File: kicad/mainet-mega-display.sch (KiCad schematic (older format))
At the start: 0 parts

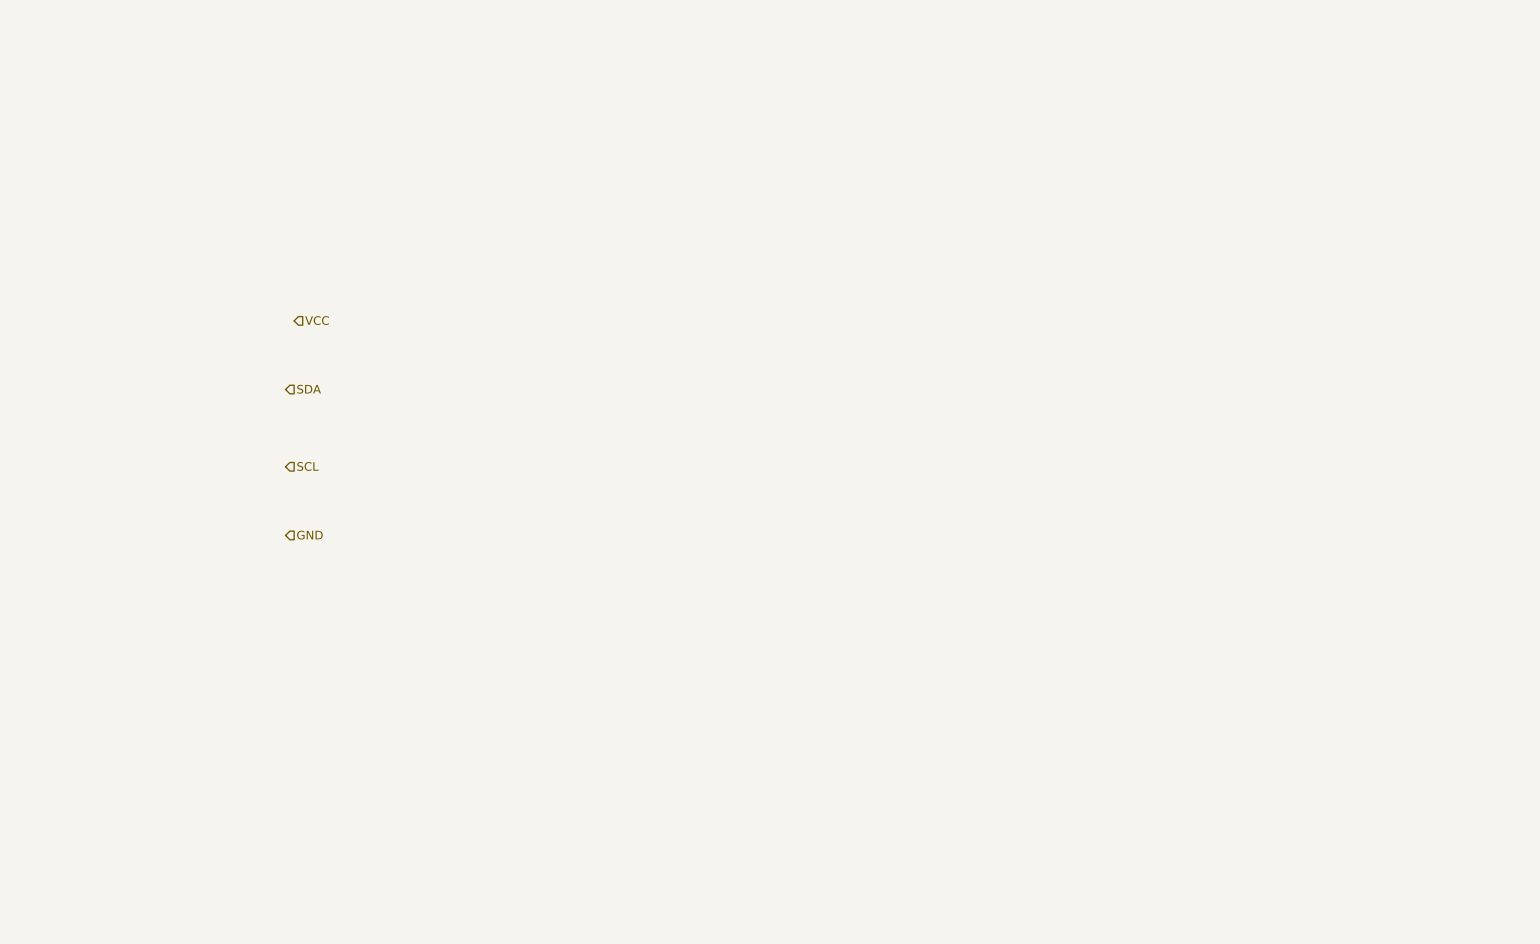
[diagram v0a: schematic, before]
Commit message: KICAD: Actualizar .sch del display Nextion
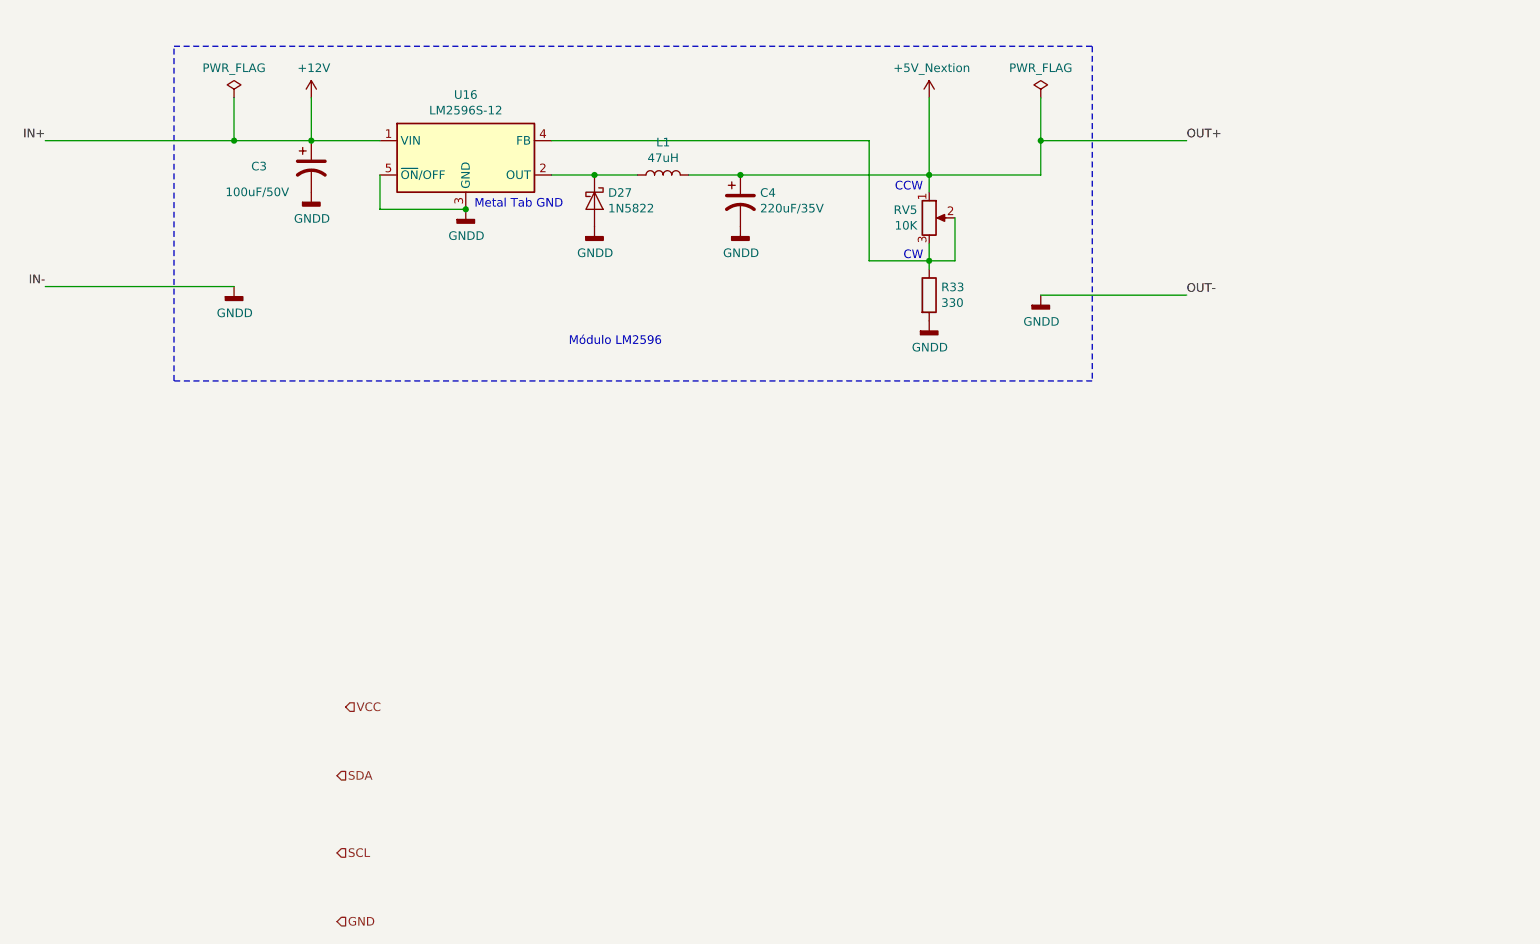
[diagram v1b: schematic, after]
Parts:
- added C3: 100uF/50V, symbol Device:CP1
- added C4: 220uF/35V, symbol Device:CP1
- added D27: 1N5822, Diode_THT:D_DO-201AD_P15.24mm_Horizontal, symbol Diode:1N5822
- added L1: 47uH, symbol Device:L
- added R33: 330, symbol Device:R
- added RV5: 10K, symbol Device:R_POT
- added U16: LM2596S-12, Package_TO_SOT_SMD:TO-263-5_TabPin3, symbol Regulator_Switching:LM2596S-12
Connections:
- new net: D27.1 (K), L1.2, U16.2 (OUT)
- new net: R33.1, RV5.2, RV5.3, U16.4 (FB)
- new net +12V: C3.1, U16.1 (VIN)
- new net +5V_Nextion: C4.1, L1.1, RV5.1
- new net GNDD: C3.2, C4.2, D27.2 (A), R33.2, U16.3 (GND), U16.5 (~ON~/OFF)
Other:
- note added: "CCW"
- note added: "CW"
- note added: "Metal Tab GND"
- note added: "Módulo LM2596"

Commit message: KICAD: Corregir pines de salida digital del Arduino para control de relés y pines de cableado con la pantalla Nextion
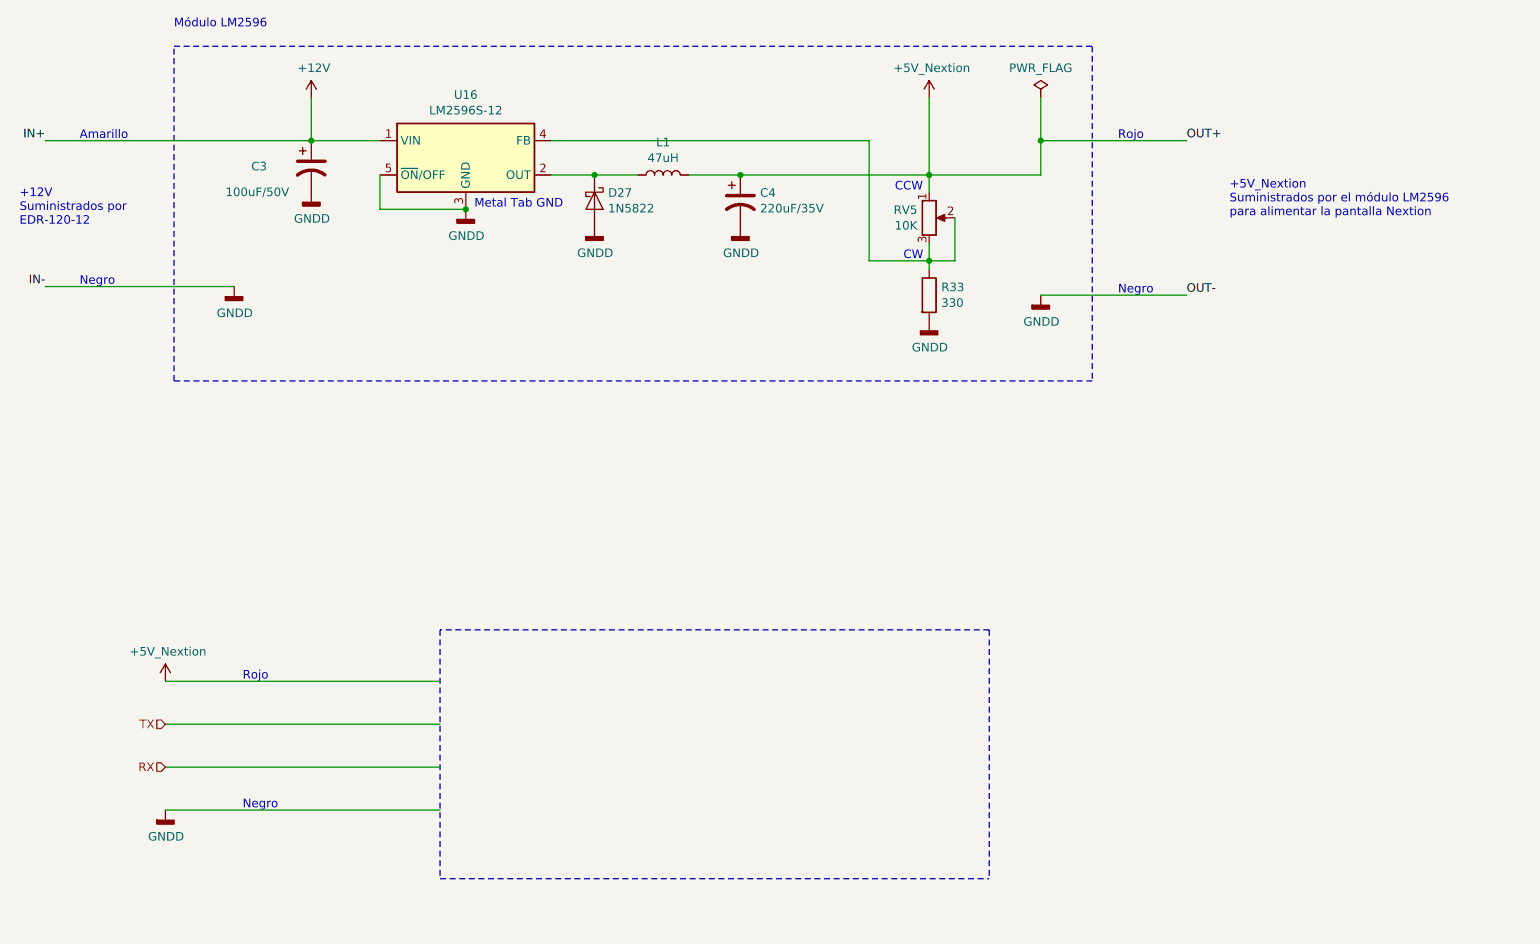
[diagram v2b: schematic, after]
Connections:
- net labels added: RX, TX
- net labels removed: GND, SCL, SDA, VCC
- wire segments 26 -> 28
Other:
- note added: "+12V\nSuministrados por\nEDR-120-12"
- note added: "+5V_Nextion\nSuministrados por el módulo LM2596\npara alimentar la pantalla Nextion"
- note added: "Amarillo"
- note added: "Negro"
- note added: "Rojo"
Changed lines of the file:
@@
 Comment4 ""
 $EndDescr
-Text HLabel 2850 4800 2    50   Input ~ 0
-VCC
-Text HLabel 2800 5200 2    50   Input ~ 0
-SDA
-Text HLabel 2800 5650 2    50   Input ~ 0
-SCL
-Text HLabel 2800 6050 2    50   Input ~ 0
-GND
+Text HLabel 1800 4900 0    50   Input ~ 0
+TX
+Text HLabel 1800 5150 0    50   Input ~ 0
+RX
 $Comp
 L nagar-power:+5V_Nextion #PWR048
@@
 	1    0    0    -1
 $EndComp
-Wire Wire Line
-	2200 1500 2650 1500
 Wire Wire Line
 	3050 1500 2650 1500
@@
 	6250 1700 6900 1700
 $Comp
-L power:PWR_FLAG #FLG0104
-U 1 1 60E05C43
-P 2200 1250
-F 0 "#FLG0104" H 2200 1325 50  0001 C CNN
-F 1 "PWR_FLAG" H 2200 1423 50  0000 C CNN
-F 2 "" H 2200 1250 50  0001 C CNN
-F 3 "~" H 2200 1250 50  0001 C CNN
-	1    2200 1250
-	1    0    0    -1
-$EndComp
-Wire Wire Line
-	2200 1250 2200 1500
-$Comp
 L power:+12V #PWR0107
 U 1 1 60E0E64F
@@
 Wire Notes Line
 	1850 2900 1850 950
-Text Notes 4150 2700 0    50   ~ 0
+Text Notes 1850 850  0    50   ~ 0
 Módulo LM2596
 Text Notes 6100 2200 0    50   ~ 0
@@
 Wire Wire Line
 	6900 2400 7750 2400
-Wire Wire Line
-	2200 1500 1100 1500
-Connection ~ 2200 1500
 Wire Wire Line
 	2200 2350 1100 2350
@@
 Text Notes 3600 1900 0    50   ~ 0
 Metal Tab GND
+Wire Wire Line
+	1100 1500 2650 1500
+Text Notes 1300 1500 0    50   ~ 0
+Amarillo
+Text Notes 1300 2350 0    50   ~ 0
+Negro
+Text Notes 7350 2400 0    50   ~ 0
+Negro
+Text Notes 7350 1500 0    50   ~ 0
+Rojo
+Wire Notes Line
+	3400 5800 6600 5800
+Wire Notes Line
+	6600 4350 3400 4350
+Wire Wire Line
+	1800 5150 3400 5150
+Wire Wire Line
+	3400 5400 1800 5400
+Text Notes 8000 1950 0    50   ~ 0
++5V_Nextion\nSuministrados por el módulo LM2596\npara alimentar la pantalla Nextion
+Text Notes 950  2000 0    50   ~ 0
++12V\nSuministrados por\nEDR-120-12
+Wire Wire Line
+	1800 4900 3400 4900
+Wire Notes Line
+	3400 4350 3400 5800
+Wire Notes Line
+	6600 4350 6600 5800
+$Comp
+L power:GNDD #PWR?
+U 1 1 60E37013
+P 1800 5400
+F 0 "#PWR?" H 1800 5150 50  0001 C CNN
+F 1 "GNDD" H 1804 5245 50  0000 C CNN
+F 2 "" H 1800 5400 50  0001 C CNN
+F 3 "" H 1800 5400 50  0001 C CNN
+	1    1800 5400
+	1    0    0    -1
+$EndComp
+$Comp
+L nagar-power:+5V_Nextion #PWR?
+U 1 1 60E37DCC
+P 1800 4650
+F 0 "#PWR?" H 1800 4500 50  0001 C CNN
+F 1 "+5V_Nextion" H 1815 4823 50  0000 C CNN
+F 2 "" H 1800 4650 50  0001 C CNN
+F 3 "" H 1800 4650 50  0001 C CNN
+	1    1800 4650
+	1    0    0    -1
+$EndComp
+Wire Wire Line
+	1800 4650 3400 4650
+Text Notes 2250 4650 0    50   ~ 0
+Rojo
+Text Notes 2250 5400 0    50   ~ 0
+Negro
 $EndSCHEMATC

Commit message: KICAD: Agregar correciones sch
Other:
- note added: "+5V"
- note added: "Azul"
- note added: "GND"
- note added: "RX"
- note added: "TX"
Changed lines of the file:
@@
 Sheet 3 22
 Title "Mainet-mega -- Diagrama de Conexiones Pantalla Nextion"
-Date "2021-04-07"
+Date "2021-07-02"
 Rev "1.0"
 Comp "Tovenca"
@@
 	6600 4350 6600 5800
 $Comp
-L power:GNDD #PWR?
+L power:GNDD #PWR0111
 U 1 1 60E37013
 P 1800 5400
-F 0 "#PWR?" H 1800 5150 50  0001 C CNN
+F 0 "#PWR0111" H 1800 5150 50  0001 C CNN
 F 1 "GNDD" H 1804 5245 50  0000 C CNN
 F 2 "" H 1800 5400 50  0001 C CNN
@@
 $EndComp
 $Comp
-L nagar-power:+5V_Nextion #PWR?
+L nagar-power:+5V_Nextion #PWR0112
 U 1 1 60E37DCC
 P 1800 4650
-F 0 "#PWR?" H 1800 4500 50  0001 C CNN
+F 0 "#PWR0112" H 1800 4500 50  0001 C CNN
 F 1 "+5V_Nextion" H 1815 4823 50  0000 C CNN
 F 2 "" H 1800 4650 50  0001 C CNN
@@
 Text Notes 2250 5400 0    50   ~ 0
 Negro
+Text Notes 2250 4900 0    50   ~ 0
+Azul
+Text Notes 2250 5150 0    50   ~ 0
+Amarillo
+Text Notes 3500 5150 0    50   ~ 0
+RX
+Text Notes 3500 4900 0    50   ~ 0
+TX
+Text Notes 3500 4650 0    50   ~ 0
++5V
+Text Notes 3500 5400 0    50   ~ 0
+GND
 $EndSCHEMATC
